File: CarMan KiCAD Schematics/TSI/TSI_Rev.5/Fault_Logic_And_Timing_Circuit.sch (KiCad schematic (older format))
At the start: 27 parts

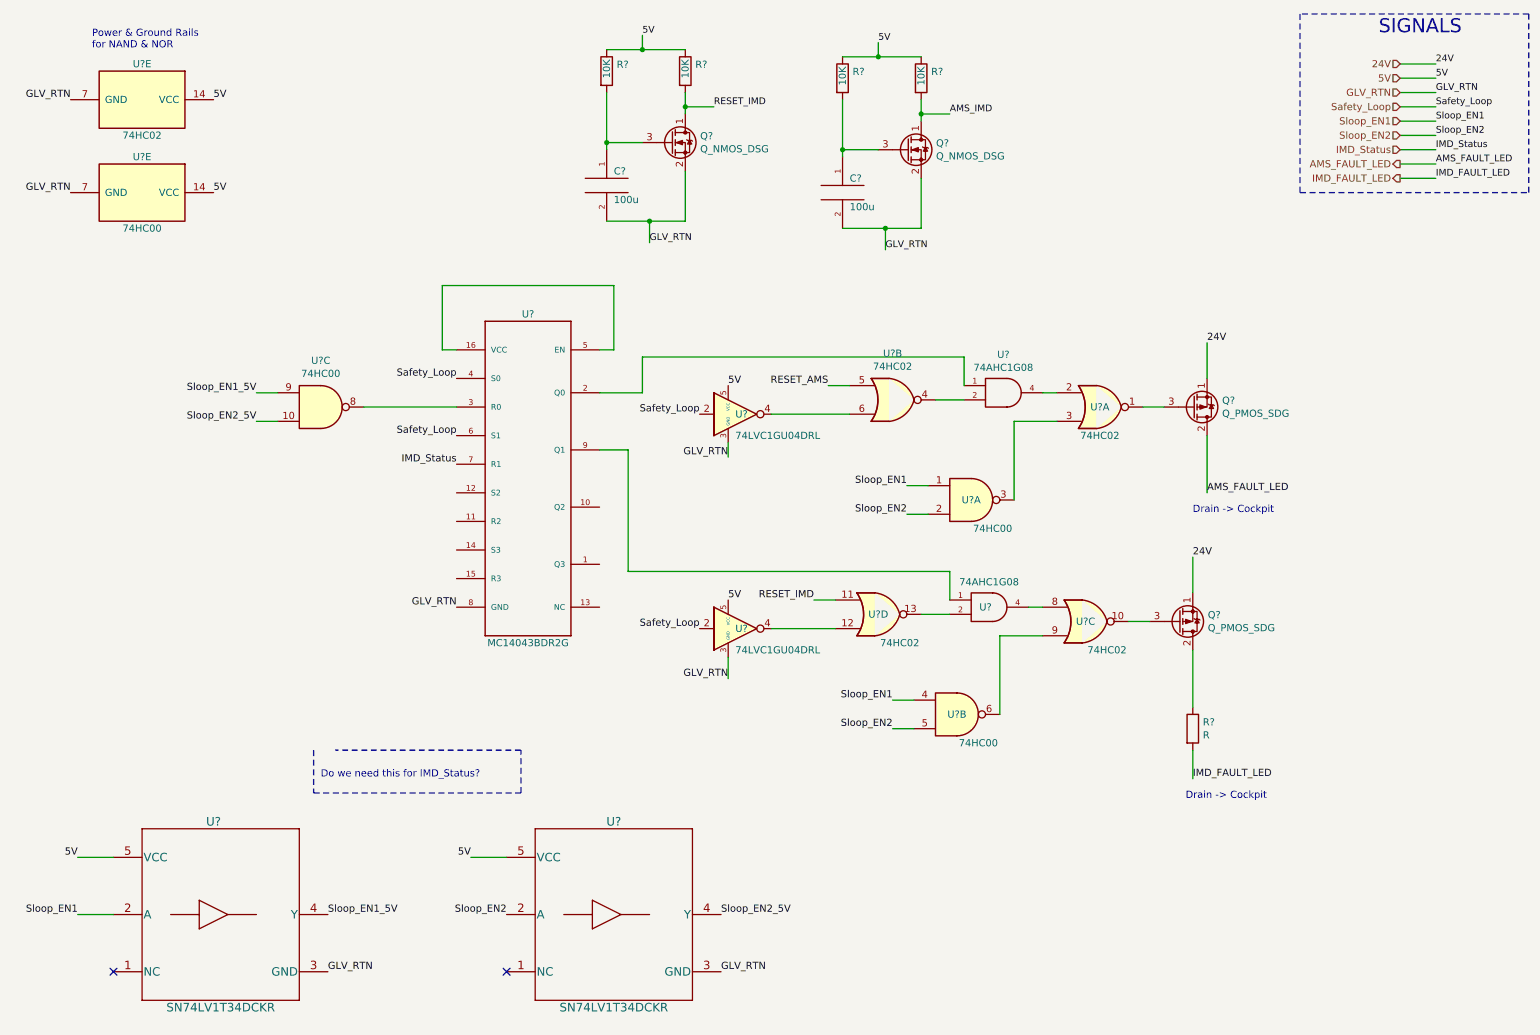
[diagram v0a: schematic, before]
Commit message: Added convertor for IMD_Status, fixed IMD/AMS led logic and Reset RC timing.
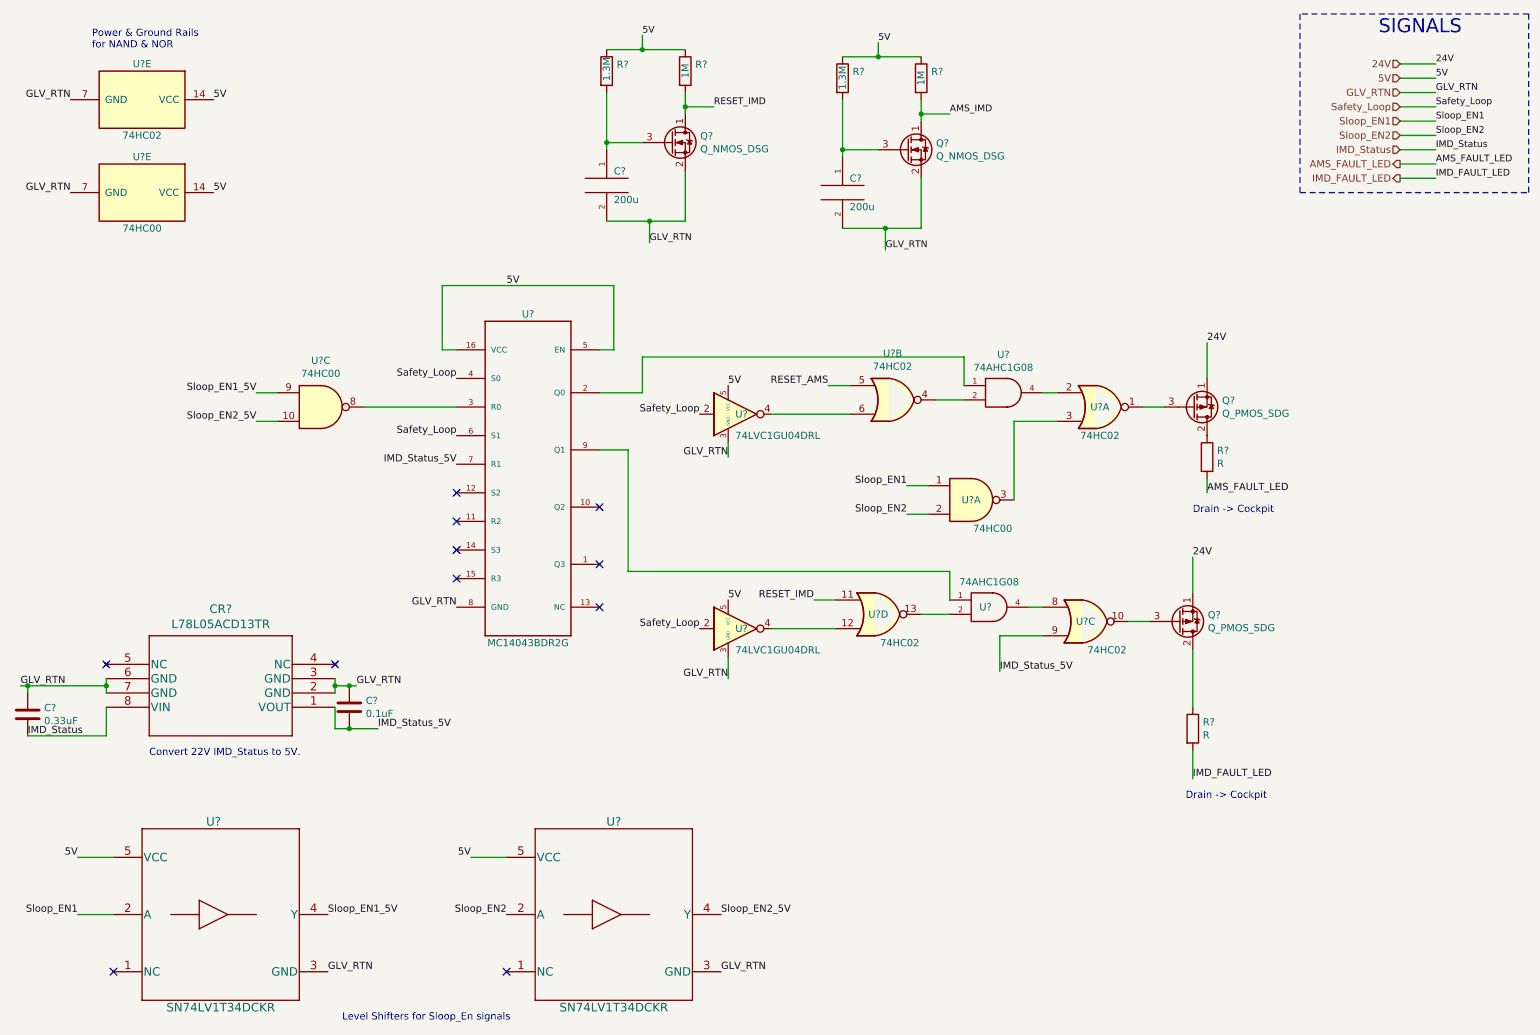
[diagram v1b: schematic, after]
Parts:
- removed U?: 74HC00, symbol CarMan_KiCAD_Library:74HC00
- added C?: 0.33uF, symbol Device:C
- added C?: 0.1uF, symbol Device:C
- added CR?: L78L05ACD13TR, SO-8_STM, symbol CarMan_KiCAD_Library:L78L05ACD13TR
- added R?: R, symbol Device:R
- C? (x2): value 100u -> 200u
- R? (x2): value 10K -> 1.3M
- R? (x2): value 10K -> 1M
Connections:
- net 5V: now also U?.16 (VCC), U?.5 (EN)
- net AMS_FAULT_LED: now also R?.2; no longer Q?.2 (D)
- net GLV_RTN: now also C?.1, C?.1, CR?.2 (GND), CR?.3 (GND), CR?.6 (GND), CR?.7 (GND)
- net IMD_Status: now also C?.2, CR?.8 (VIN); no longer U?.7 (R1)
- net IMD_Status_5V: now reaches U?.9
- net IMD_Status_5V: now also U?.7 (R1), C?.2, CR?.1 (VOUT)
- new net: Q?.2 (D), R?.1
- no-connect marks 2 -> 11
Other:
- note added: "Convert 22V IMD_Status to 5V."
- note added: "Level Shifters for Sloop_En signals"
- note removed: "Do we need this for IMD_Status?"
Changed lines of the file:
@@
 Wire Wire Line
 	8900 2800 8900 3050
-Wire Wire Line
-	8900 3450 8900 3850
 Text Notes 8800 4000 0    50   ~ 0
 Drain -> Cockpit
@@
 Wire Wire Line
 	7650 4650 7750 4650
-Text Label 6700 5300 2    50   ~ 0
-Sloop_EN1
-Wire Wire Line
-	6700 5300 6850 5300
-Wire Wire Line
-	6700 5500 6850 5500
-Text Label 6700 5500 2    50   ~ 0
-Sloop_EN2
 Wire Wire Line
 	7750 4850 7450 4850
-Wire Wire Line
-	7450 4850 7450 5400
 Wire Wire Line
 	8500 4750 8350 4750
@@
 	2250 3350 2400 3350
 Text Label 3650 3650 2    50   ~ 0
-IMD_Status
+IMD_Status_5V
 Wire Wire Line
 	3000 3250 3650 3250
@@
 F 3 "http://www.ti.com/lit/gpn/sn74hc02" H 6600 4700 50  0001 C CNN
 	4    6600 4700
-	1    0    0    -1
-$EndComp
-$Comp
-L CarMan_KiCAD_Library:74HC00 U?
-U 2 1 5FA8940E
-P 7150 5400
-F 0 "U?" H 7150 5400 50  0000 C CNN
-F 1 "74HC00" H 7300 5200 50  0000 C CNN
-F 2 "" H 7150 5400 50  0001 C CNN
-F 3 "http://www.ti.com/lit/gpn/sn74hc00" H 7150 5400 50  0001 C CNN
-	2    7150 5400
 	1    0    0    -1
 $EndComp
@@
 Text Label 2750 6800 0    50   ~ 0
 Sloop_EN1_5V
-Text Notes 2700 5850 0    50   ~ 0
-Do we need this for IMD_Status?
-Wire Notes Line
-	2650 5650 2650 5950
-Wire Notes Line
-	2650 5950 4100 5950
-Wire Notes Line
-	4100 5950 4100 5650
-Wire Notes Line
-	4100 5650 2800 5650
 Text Label 1950 1100 0    50   ~ 0
 5V
@@
 P 4700 900
 F 0 "R?" H 4770 946 50  0000 L CNN
-F 1 "10K" V 4700 850 50  0000 L CNN
+F 1 "1.3M" V 4700 830 50  0000 L CNN
 F 2 "" V 4630 900 50  0001 C CNN
 F 3 "~" H 4700 900 50  0001 C CNN
@@
 P 5250 900
 F 0 "R?" H 5320 946 50  0000 L CNN
-F 1 "10K" V 5250 850 50  0000 L CNN
+F 1 "1M" V 5250 850 50  0000 L CNN
 F 2 "" V 5180 900 50  0001 C CNN
 F 3 "~" H 5250 900 50  0001 C CNN
@@
 P 4700 1700
 F 0 "C?" H 4750 1800 50  0000 L CNN
-F 1 "100u" H 4750 1600 50  0000 L CNN
+F 1 "200u" H 4750 1600 50  0000 L CNN
 F 2 "" H 4700 1700 50  0001 C CNN
 F 3 "~" H 4700 1700 50  0001 C CNN
@@
 P 6350 950
 F 0 "R?" H 6420 996 50  0000 L CNN
-F 1 "10K" V 6350 900 50  0000 L CNN
+F 1 "1.3M" V 6350 869 50  0000 L CNN
 F 2 "" V 6280 950 50  0001 C CNN
 F 3 "~" H 6350 950 50  0001 C CNN
@@
 P 6900 950
 F 0 "R?" H 6970 996 50  0000 L CNN
-F 1 "10K" V 6900 900 50  0000 L CNN
+F 1 "1M" V 6900 900 50  0000 L CNN
 F 2 "" V 6830 950 50  0001 C CNN
 F 3 "~" H 6900 950 50  0001 C CNN
@@
 P 6350 1750
 F 0 "C?" H 6400 1850 50  0000 L CNN
-F 1 "100u" H 6400 1650 50  0000 L CNN
+F 1 "200u" H 6400 1650 50  0000 L CNN
 F 2 "" H 6350 1750 50  0001 C CNN
 F 3 "~" H 6350 1750 50  0001 C CNN
@@
 	1    0    0    -1
 $EndComp
+$Comp
+L Device:R R?
+U 1 1 5F9E6F79
+P 8900 3600
+F 0 "R?" H 8970 3646 50  0000 L CNN
+F 1 "R" H 8970 3555 50  0000 L CNN
+F 2 "" V 8830 3600 50  0001 C CNN
+F 3 "~" H 8900 3600 50  0001 C CNN
+	1    8900 3600
+	1    0    0    -1
+$EndComp
+Wire Wire Line
+	8900 3750 8900 3850
+Text Notes 2850 7550 0    50   ~ 0
+Level Shifters for Sloop_En signals
+$Comp
+L CarMan_KiCAD_Library:L78L05ACD13TR CR?
+U 1 1 5F9F52BF
+P 2800 5350
+F 0 "CR?" H 3600 4663 60  0000 C CNN
+F 1 "L78L05ACD13TR" H 3600 4769 60  0000 C CNN
+F 2 "SO-8_STM" H 3600 5590 60  0001 C CNN
+F 3 "" H 2800 5350 60  0000 C CNN
+	1    2800 5350
+	-1   0    0    1
+$EndComp
+NoConn ~ 1200 5050
+NoConn ~ 2800 5050
+Wire Wire Line
+	1200 5150 1200 5200
+Connection ~ 1200 5200
+Wire Wire Line
+	1200 5200 1200 5250
+Text Label 600  5200 0    50   ~ 0
+GLV_RTN
+Text Label 650  5550 0    50   ~ 0
+IMD_Status
+Wire Wire Line
+	2800 5150 2800 5200
+Wire Wire Line
+	2800 5200 2900 5200
+Connection ~ 2800 5200
+Wire Wire Line
+	2800 5200 2800 5250
+Text Label 2950 5200 0    50   ~ 0
+GLV_RTN
+Wire Wire Line
+	600  5200 650  5200
+Wire Wire Line
+	2800 5350 2800 5500
+Wire Wire Line
+	2800 5500 2900 5500
+Text Label 3100 5500 0    50   ~ 0
+IMD_Status_5V
+Wire Wire Line
+	1200 5350 1200 5550
+Wire Wire Line
+	1200 5550 650  5550
+$Comp
+L Device:C C?
+U 1 1 5FA18C24
+P 650 5400
+F 0 "C?" H 765 5446 50  0000 L CNN
+F 1 "0.33uF" H 765 5355 50  0000 L CNN
+F 2 "" H 688 5250 50  0001 C CNN
+F 3 "~" H 650 5400 50  0001 C CNN
+	1    650  5400
+	1    0    0    -1
+$EndComp
+$Comp
+L Device:C C?
+U 1 1 5FA196B8
+P 2900 5350
+F 0 "C?" H 3015 5396 50  0000 L CNN
+F 1 "0.1uF" H 3015 5305 50  0000 L CNN
+F 2 "" H 2938 5200 50  0001 C CNN
+F 3 "~" H 2900 5350 50  0001 C CNN
+	1    2900 5350
+	1    0    0    -1
+$EndComp
+Connection ~ 2900 5200
+Wire Wire Line
+	2900 5200 2950 5200
+Connection ~ 2900 5500
+Wire Wire Line
+	2900 5500 3100 5500
+Wire Wire Line
+	650  5250 650  5200
+Connection ~ 650  5200
+Wire Wire Line
+	650  5200 1200 5200
+Text Label 7450 5100 0    50   ~ 0
+IMD_Status_5V
+Wire Wire Line
+	7450 5100 7450 4850
+Text Notes 1500 5700 0    50   ~ 0
+Convert 22V IMD_Status to 5V.
+Text Label 4000 2400 0    50   ~ 0
+5V
+NoConn ~ 4650 4650
+NoConn ~ 4650 4350
+NoConn ~ 4650 3950
+NoConn ~ 3650 3850
+NoConn ~ 3650 4050
+NoConn ~ 3650 4250
+NoConn ~ 3650 4450
 $EndSCHEMATC

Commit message: Removed CAN Transciever from CAN & GLV Power, edited net listing on PCDC Circuit regarding Safety_Loop Iso and extraneous connector
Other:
- note added: "FAULT LOGIC \n& TIMING CIRCUIT"
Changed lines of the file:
@@
 NoConn ~ 3650 4250
 NoConn ~ 3650 4450
+Text Notes 7350 7050 0    157  ~ 0
+FAULT LOGIC \n& TIMING CIRCUIT
 $EndSCHEMATC
